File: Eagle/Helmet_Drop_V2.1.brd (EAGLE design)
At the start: 106.4 x 172.7 mm, 30 parts, among them Q3 MOSFET-NCH, Q4 MOSFET-NCH, Q5 MOSFET-NCH, U1 TH_DS_LIBRARIES_ITSYBITSY_5V, X1 MSTBA4, X2 TH_DS_LIBRARIES_MSTBA4

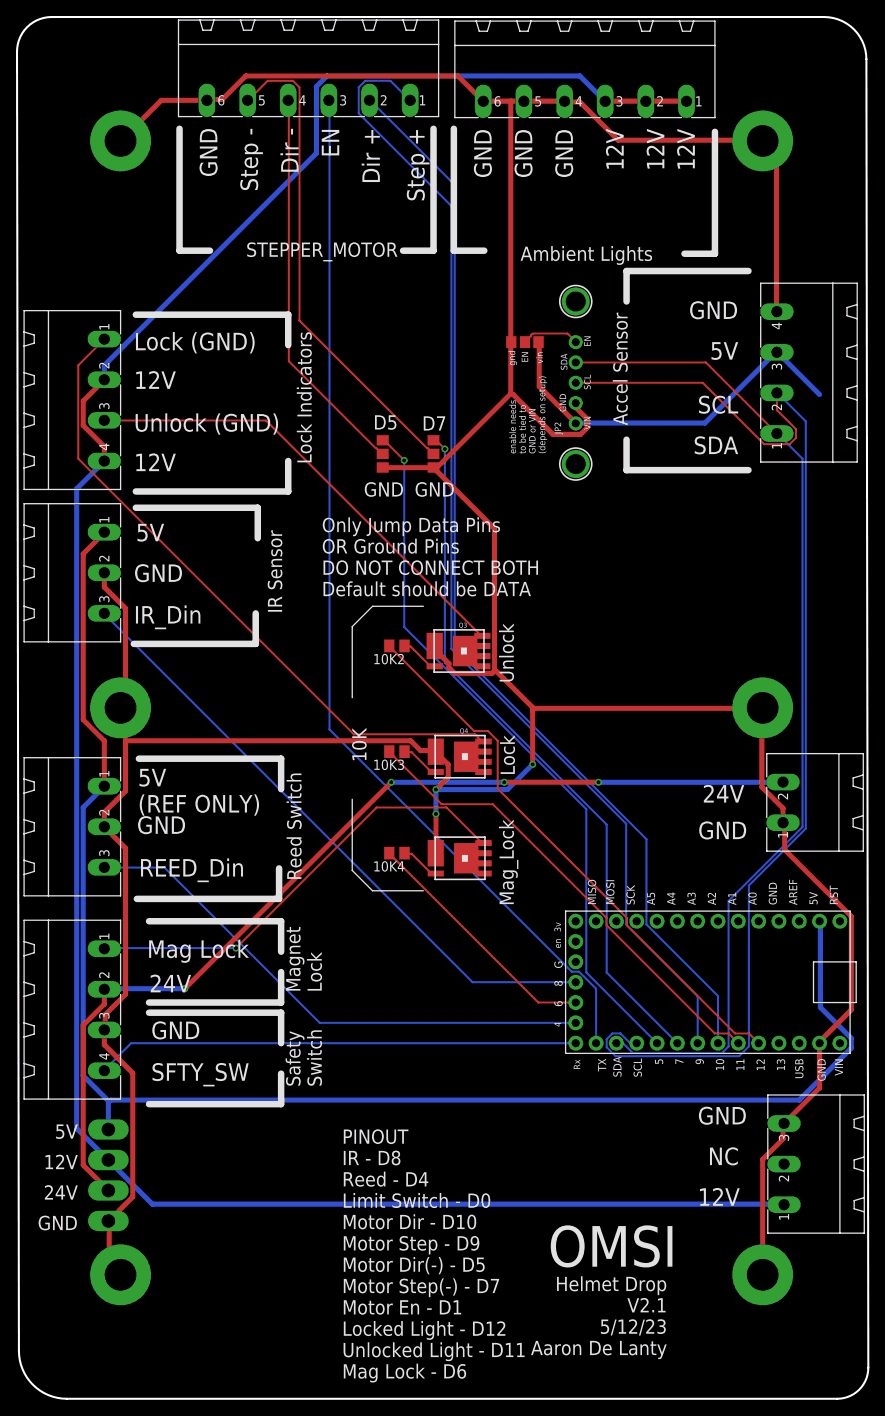
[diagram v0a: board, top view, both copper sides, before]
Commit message: updated indicator lights
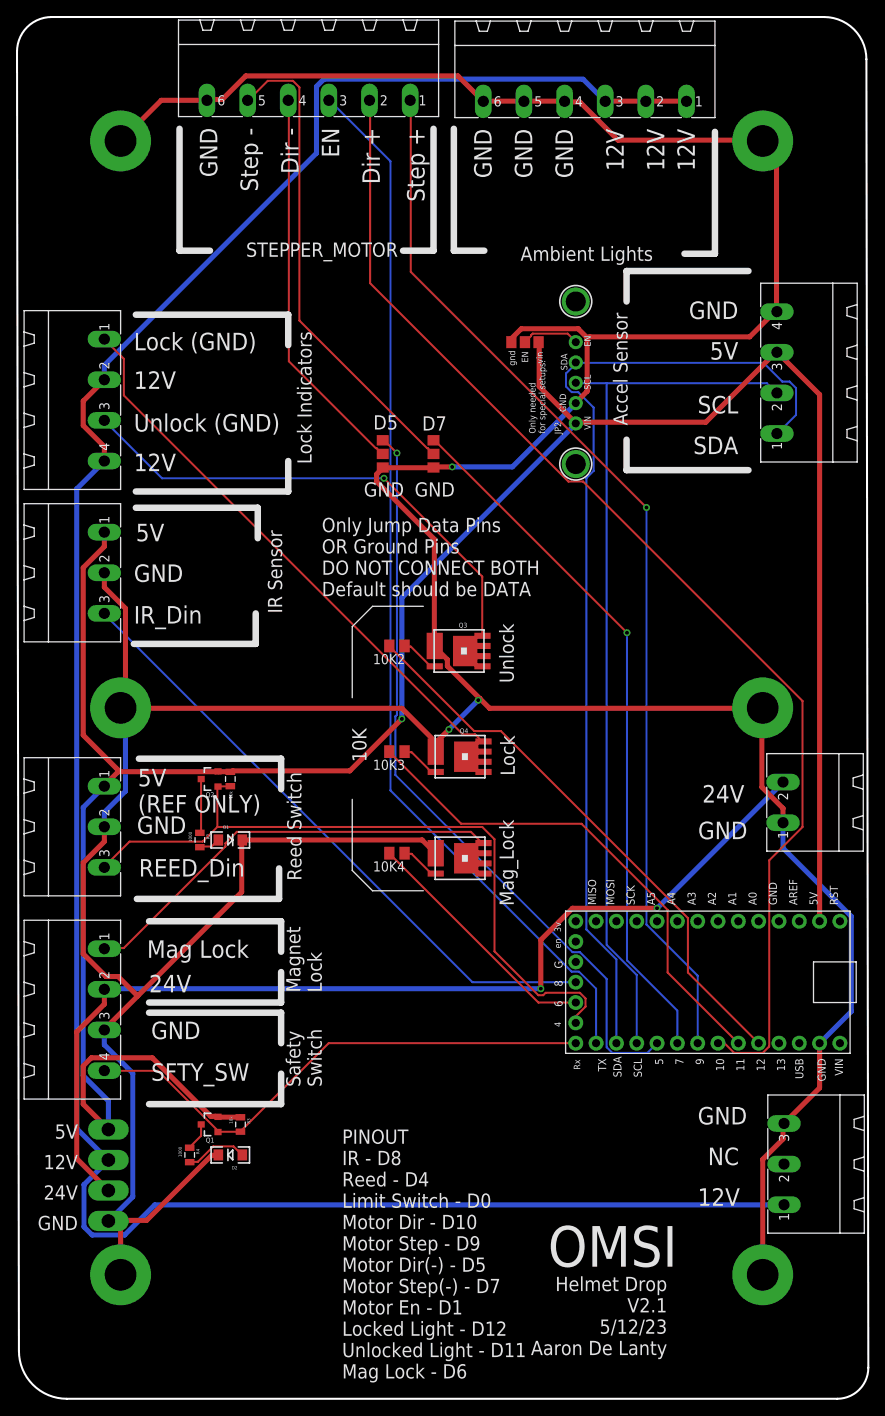
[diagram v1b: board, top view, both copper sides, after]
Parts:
- added D1, D2: (no value), SparkFun-LED:LED-1206
- added Q1, Q2: 2.5A/30V/105mΩ, SparkFun-DiscreteSemi:SOT23-3@1
- added R1, R3: 10k, SparkFun-Passives:0805
- added R2, R4: 1000, SparkFun-Passives:0805
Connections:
- removed net D0: U1.RX, X1.4
- removed net D4: REED_IN.3, U1.D4
- new net N$2: Q2.3, R2.1
- new net N$3: Q1.3, R4.1
- new net N$4: D2.A, R4.2
- new net N$5: D1.A, R2.2
- new net REEDIN: Q2.1, R1.2, REED_IN.3, U1.D4
- new net SAFETYSWITCH: Q1.1, R3.2, U1.RX, X1.4
- net 5V: now also Q1.2, Q2.2, R1.1, R3.1
- net GND: now also D1.C, D2.C
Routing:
- net REEDIN: track 0.00 -> 89.8 mm
- net 5V: track 240.3 -> 311.5 mm, vias 0 -> 1
- net D4: track 67.0 -> 0.00 mm
- net SAFETYSWITCH: track 0.00 -> 66.8 mm
- net D0: track 60.4 -> 0.00 mm
- net GND: track 504.6 -> 551.2 mm
- net SCL: track 148.1 -> 109.8 mm
- net D10: track 135.9 -> 150.8 mm
- net D9: track 144.8 -> 132.8 mm, vias 0 -> 1
- net 12V: track 285.4 -> 297.4 mm
- net N$10: track 81.6 -> 70.9 mm
- net N$4: track 0.00 -> 7.85 mm
- net N$2: track 0.00 -> 6.82 mm
- net D5: track 89.7 -> 95.4 mm
- net N$7: track 58.5 -> 62.8 mm, vias 0 -> 1
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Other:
- board text added: "Only needed for special setups."
- board text removed: "enable needs to be tied to GND or VIN (depends on setup)"

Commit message: cleanup
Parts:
- removed JP2: (no value), microbuilder:1X05_ROUND_70
- removed S10, S11, S12, S5, S7, S9: STANDOFF_ELECTRICAL5-32, th_libraries:STANDOFF_ELECTRICAL_5_32
- removed U$19, U$21: MOUNTINGHOLE2.5, microbuilder:MOUNTINGHOLE_2.5_PLATED
- added S1, S2, S3, S4, S6, S8: GND_HOLE, OMSI_Default_V1:GND_HOLE
- added TP3, TP4: TEST_POINTTP_15TH_THRU, OMSI_Default_V1:TESTPOINT_HEADER_1X01
- added U$1: I2C_EXTENDER, OMSI_Default_V1:I2C_EXTENDER
- 10K2, 10K3, 10K4: device adafruit:M0805 -> OMSI_Default_V1:SMD_RESISTOR_0805
- 12V_IN, IR_IN, REED_IN: value MSTBA3 -> PHOENIX_508_3PIN; device con-phoenix-508:MSTBA3 -> OMSI_Default_V1:PHOENIX_508_3PIN
- 24V: value MSTBA2 -> PHOENIX_508_2PIN; device th_libraries:MSTBA2 -> OMSI_Default_V1:PHOENIX_508_2PIN
- AUXILLARY_LIGHTS1, STEPPER_MOTOR: value MSTBA6 -> PHOENIX_508_6PIN; device con-phoenix-508:MSTBA6 -> OMSI_Default_V1:PHOENIX_508_6PIN
- D1, D2: device SparkFun-LED:LED-1206 -> OMSI_Default_V1:SMD_LED-1206
- JMP1, JMP2: value 0R-JUMPB -> SMD_JUMPERA; device jump-0r-smd:B0R-JMP -> OMSI_Default_V1:JUMPER_A-OR
- JMP3: value 0R-JUMPA -> SMD_JUMPERA; device jump-0r-smd:A0R-JMP -> OMSI_Default_V1:JUMPER_A-OR
- LOCK_LIGHTS: value MSTBA4 -> PHOENIX_508_4PIN; device th_libraries:MSTBA4 -> OMSI_Default_V1:PHOENIX_508_4PIN
- Q1, Q2: value 2.5A/30V/105mΩ -> MOSFET-PCHIRLML9301TRPBF; device SparkFun-DiscreteSemi:SOT23-3@1 -> OMSI_Default_V1:SOT23-3
- Q3, Q4, Q5: value MOSFET-NCH -> 310mA/60V/1.6Ω; device th_ds_libraries:SO-8_POWER_PAK -> OMSI_Default_V1:SO-8_POWER_PAK
- R1, R2, R3, R4: device SparkFun-Passives:0805 -> OMSI_Default_V1:SMD_RESISTOR_0805
- TP1, TP2: value PTR2 -> TEST_POINTTP_15TH_THRU; device testpad:P2-38-17 -> OMSI_Default_V1:TESTPOINT_HEADER_1X01
- U1: value TH_DS_LIBRARIES_ITSYBITSY_5V -> ADAFRUIT_ITSYBITSY_5V; device Helmet_Drop_V1.5:TH_DS_LIBRARIES_ADAFRUIT_LENOARDO -> OMSI_Default_V1:ADAFRUIT_ITSYBITSY
- X1: value MSTBA4 -> PHOENIX_508_4PIN; device con-phoenix-508:MSTBA4 -> OMSI_Default_V1:PHOENIX_508_4PIN
- X2: value TH_DS_LIBRARIES_MSTBA4 -> PHOENIX_508_4PIN; device OMSI_Default_V1:TH_DS_LIBRARIES_MSTBA4 -> OMSI_Default_V1:PHOENIX_508_4PIN
- moved TP2 10.0 mm to (20.6, 23.2), turned to 0 degrees
- moved U1 6.35 mm to (97.8, 54.6)
- moved TP1 2.87 mm to (20.6, 27.1), turned to 0 degrees
- moved D1 2.54 mm to (40.6, 71.1)
- moved R2 1.27 mm to (35.6, 71.1), turned to 0 degrees
- moved R1 1.27 mm to (39.4, 78.7)
- turned JMP1 to 0 degrees
- turned JMP2 to 0 degrees
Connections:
- net 12V: now also TP4.P$1; no longer TP2.TP-2
- net 24V: now also TP1.P$1; no longer TP1.TP-1
- net 5V: now also TP3.P$1, U$1.VIN; no longer JP2.1, TP2.TP-1
- net D5: now also JMP1.1; no longer JMP1.3
- net D7: now also JMP2.1; no longer JMP2.3
- net EN: now also U$1.EN; no longer JP2.5
- net GND: now also JMP1.3, JMP2.3, S1.P$1, S2.P$1, S3.P$1, S4.P$1, S6.P$1, S8.P$1, TP2.P$1, U$1.GND; no longer JMP1.1, JMP2.1, JP2.2, S10.P1, S11.P1, S12.P1, S5.P1, S7.P1, S9.P1, TP1.TP-2
- net SCL: now also U$1.SCL; no longer JP2.3
- net SDA: now also U$1.SDA; no longer JP2.4
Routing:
- net D9: track 132.8 -> 162.4 mm, vias 1 -> 0
- net D10: track 150.8 -> 135.1 mm, vias 0 -> 1
- net 24V: track 127.4 -> 136.1 mm, vias 2 -> 1
- net 5V: track 311.5 -> 320.0 mm
- net N$10: track 70.9 -> 79.1 mm
- net SDA: track 125.0 -> 132.1 mm
- net D5: track 95.4 -> 88.4 mm, vias 1 -> 2
- net D11: track 63.3 -> 59.0 mm
- net N$7: track 62.8 -> 58.5 mm, vias 1 -> 0
- net D12: track 70.7 -> 73.8 mm
- net GND: track 551.2 -> 552.8 mm
- net 12V: track 297.4 -> 295.9 mm
- net D7: track 88.1 -> 86.8 mm
- net D1: track 132.3 -> 131.1 mm
- net N$5: track 6.82 -> 7.76 mm
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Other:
- board text removed: "VIN"
- board text removed: "vin"
